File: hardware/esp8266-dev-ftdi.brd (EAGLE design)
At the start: 50 x 50 mm, 58 parts, among them CON1 USBMICRO-NO_CENTER-LONG_PADS

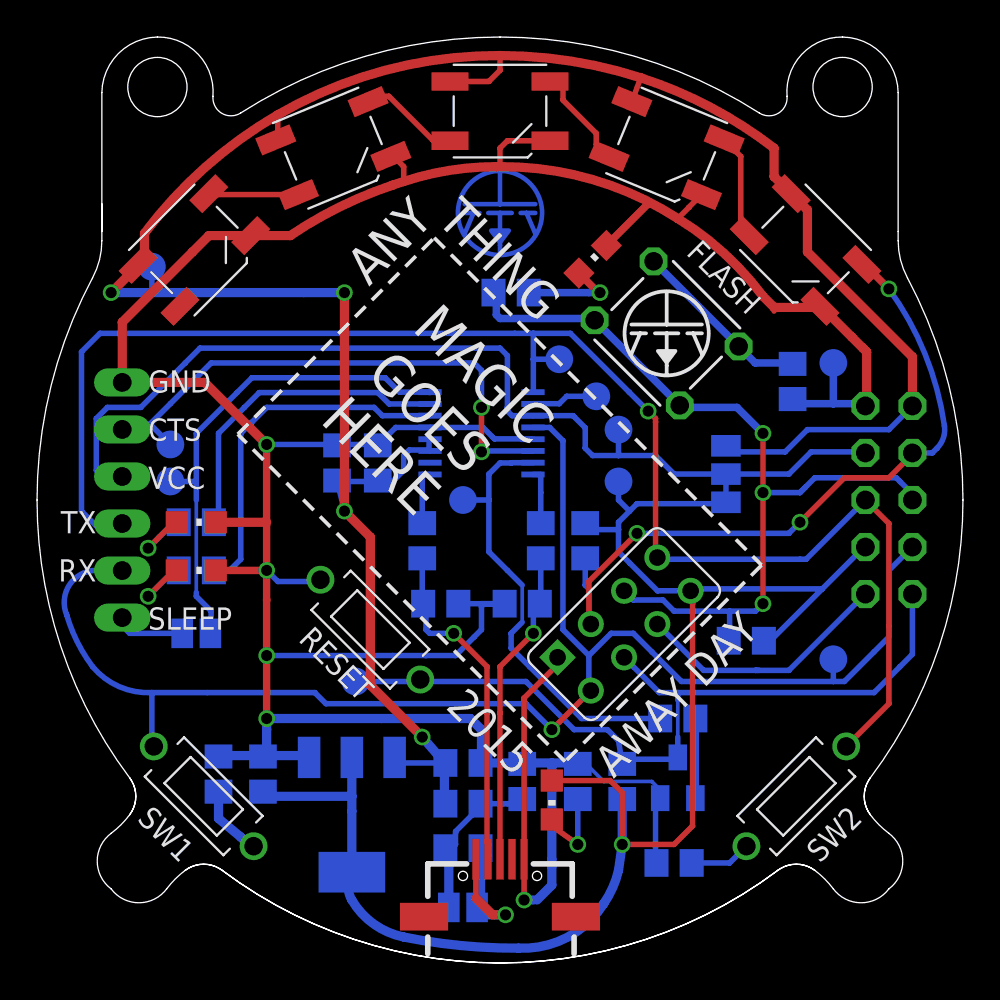
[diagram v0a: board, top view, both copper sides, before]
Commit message: added decoupling caps for leds
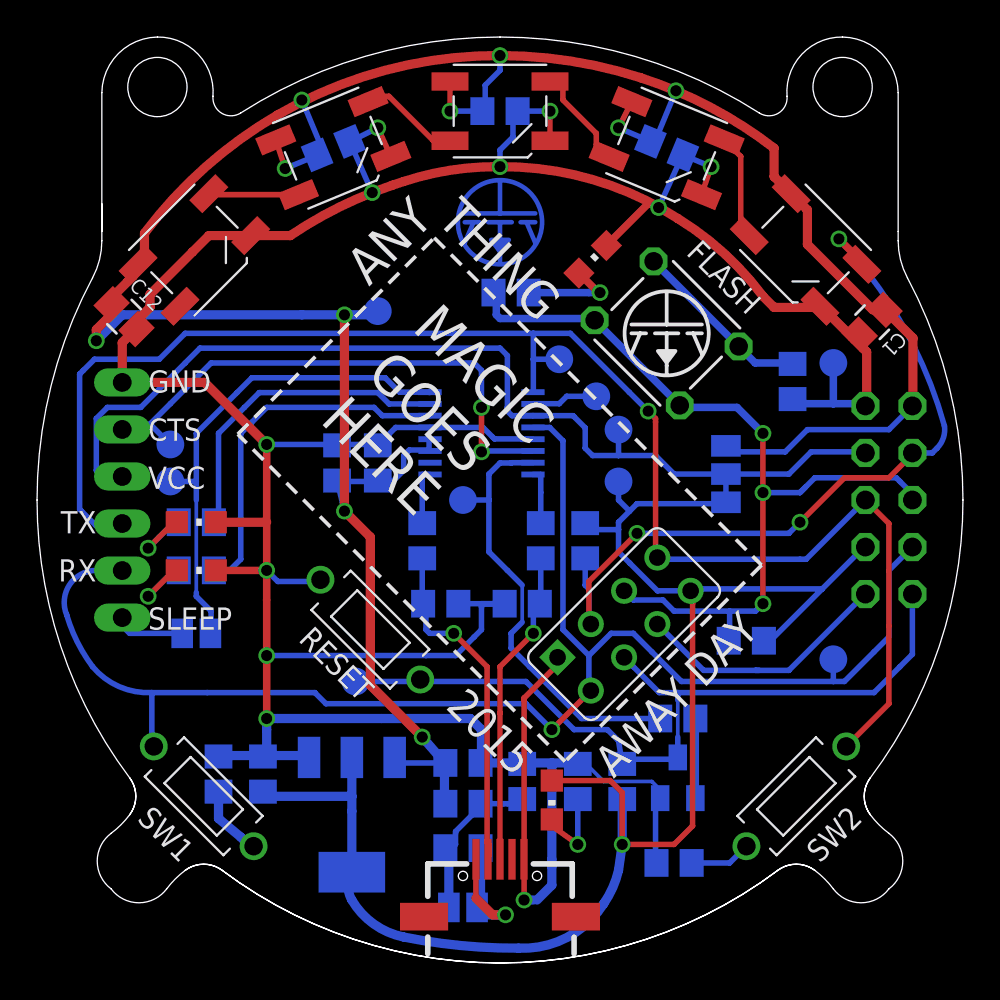
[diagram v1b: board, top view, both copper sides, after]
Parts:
- added C1, C10, C11, C12, C9: 100n, p.peter-rcl:C0805
- moved 5V 12.4 mm to (18.4, 35.2)
- moved U$1 0.50 mm to (25.0, 40.0)
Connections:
- net +5V: now also C1.1, C10.1, C11.1, C12.1, C9.1
- net GND: now also C1.2, C10.2, C11.2, C12.2, C9.2
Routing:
- net +5V: track 134.8 -> 157.2 mm, vias 4 -> 10
- net GND: track 200.6 -> 214.3 mm, vias 5 -> 11
- net IO2: track 39.1 -> 42.8 mm
- net TX: track 84.1 -> 83.5 mm

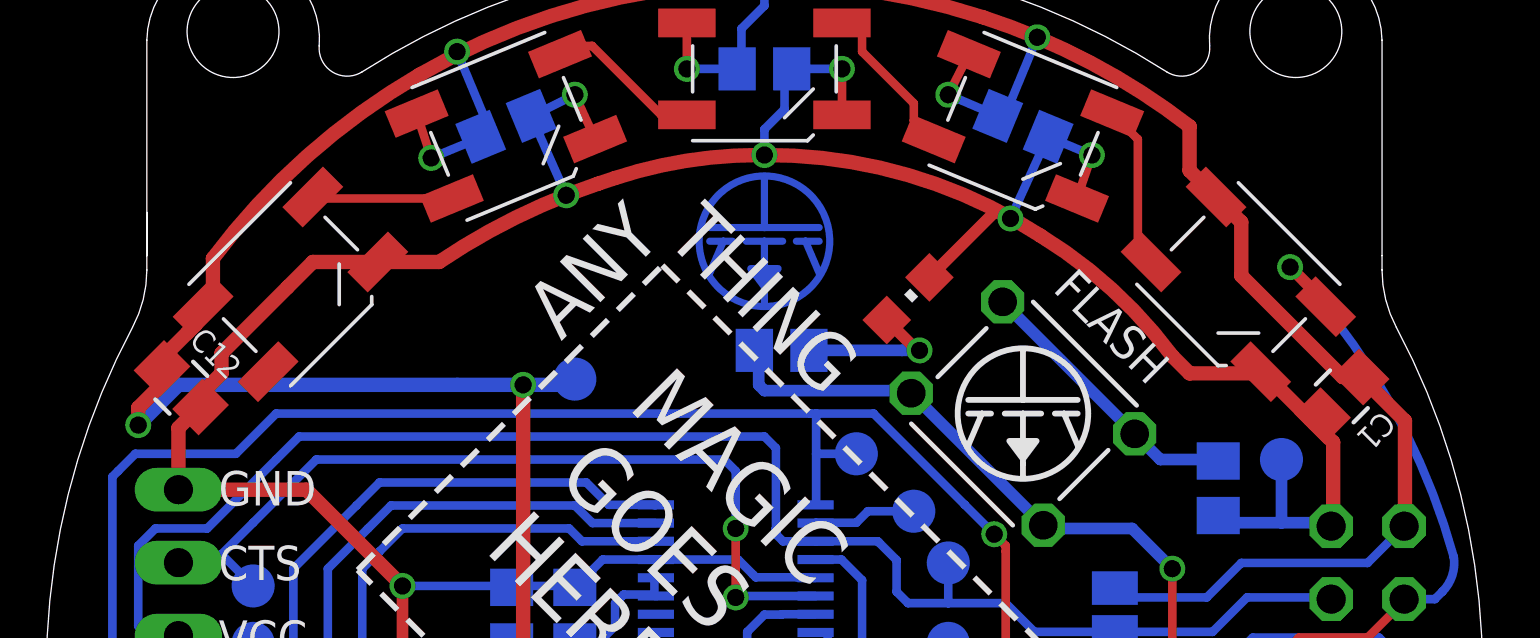
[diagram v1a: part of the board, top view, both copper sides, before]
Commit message: changed bottom values to place layer
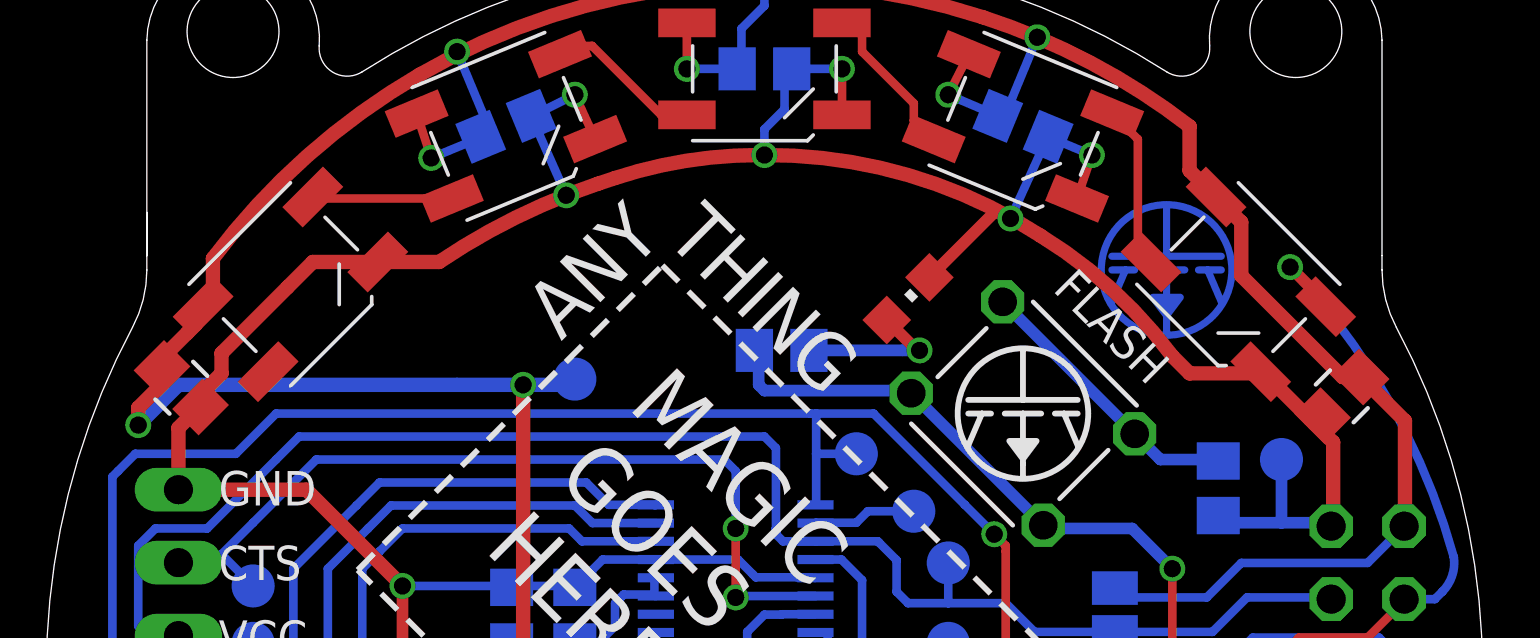
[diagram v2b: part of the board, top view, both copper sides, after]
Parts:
- moved U$1 14.0 mm to (39.0, 39.0)

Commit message: cosmetics
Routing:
- net VCCIO: track 56.8 -> 55.2 mm
- net +3V3: track 89.1 -> 90.3 mm
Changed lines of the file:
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@@
 <setting verticaltext="up"/>
 </settings>
-<grid distance="1" unitdist="mm" unit="mm" style="lines" multiple="1" display="yes" altdistance="0.1" altunitdist="mm" altunit="mm"/>
+<grid distance="0.1" unitdist="mm" unit="mm" style="lines" multiple="1" display="yes" altdistance="0.05" altunitdist="mm" altunit="mm"/>
 <layers>
-<layer number="1" name="Top" color="4" fill="1" visible="no" active="yes"/>
+<layer number="1" name="Top" color="4" fill="1" visible="yes" active="yes"/>
 <layer number="16" name="Bottom" color="1" fill="1" visible="no" active="yes"/>
-<layer number="17" name="Pads" color="2" fill="1" visible="no" active="yes"/>
-<layer number="18" name="Vias" color="2" fill="1" visible="no" active="yes"/>
-<layer number="19" name="Unrouted" color="6" fill="1" visible="no" active="yes"/>
-<layer number="20" name="Dimension" color="15" fill="1" visible="no" active="yes"/>
-<layer number="21" name="tPlace" color="7" fill="1" visible="no" active="yes"/>
+<layer number="17" name="Pads" color="2" fill="1" visible="yes" active="yes"/>
+<layer number="18" name="Vias" color="2" fill="1" visible="yes" active="yes"/>
+<layer number="19" name="Unrouted" color="6" fill="1" visible="yes" active="yes"/>
+<layer number="20" name="Dimension" color="15" fill="1" visible="yes" active="yes"/>
+<layer number="21" name="tPlace" color="7" fill="1" visible="yes" active="yes"/>
 <layer number="22" name="bPlace" color="7" fill="1" visible="no" active="yes"/>
-<layer number="23" name="tOrigins" color="15" fill="1" visible="no" active="yes"/>
+<layer number="23" name="tOrigins" color="15" fill="1" visible="yes" active="yes"/>
 <layer number="24" name="bOrigins" color="15" fill="1" visible="no" active="yes"/>
-<layer number="25" name="tNames" color="7" fill="1" visible="no" active="yes"/>
+<layer number="25" name="tNames" color="7" fill="1" visible="yes" active="yes"/>
 <layer number="26" name="bNames" color="7" fill="1" visible="no" active="yes"/>
 <layer number="27" name="tValues" color="7" fill="1" visible="yes" active="yes"/>
-<layer number="28" name="bValues" color="7" fill="1" visible="yes" active="yes"/>
-<layer number="29" name="tStop" color="7" fill="3" visible="no" active="yes"/>
+<layer number="28" name="bValues" color="7" fill="1" visible="no" active="yes"/>
+<layer number="29" name="tStop" color="7" fill="3" visible="yes" active="yes"/>
 <layer number="30" name="bStop" color="7" fill="6" visible="no" active="yes"/>
 <layer number="31" name="tCream" color="7" fill="4" visible="no" active="yes"/>
@@
 <text x="43.2" y="22" size="1.2" layer="22" font="vector" ratio="15" rot="MR270" align="bottom-center">3V3</text>
 <text x="44.8" y="18.6" size="1.2" layer="22" font="vector" ratio="15" rot="MR270" align="center-left">16</text>
-<text x="48.4" y="27.6" size="1.2" layer="22" font="vector" ratio="15" rot="MR270" align="top-center">2</text>
-<text x="48.4" y="25" size="1.2" layer="22" font="vector" ratio="15" rot="MR270" align="top-center">0</text>
-<text x="48.4" y="22.4" size="1.2" layer="22" font="vector" ratio="15" rot="MR270" align="top-center">RX</text>
+<text x="48.4" y="27.6" size="1" layer="22" font="vector" ratio="15" rot="MR270" align="top-center">2</text>
+<text x="48.4" y="25" size="1" layer="22" font="vector" ratio="15" rot="MR270" align="top-center">0</text>
+<text x="48.4" y="22.7" size="1" layer="22" font="vector" ratio="15" rot="MR270" align="top-center">RX</text>
 <text x="47.2" y="18.8" size="1.2" layer="22" font="vector" ratio="15" rot="MR270" align="center-left">RES</text>
 <text x="17.6" y="36" size="1.7" layer="22" font="vector" ratio="15" rot="MR0">ESP 8266
@@
 </class>
 </classes>
-<designrules name="Elecrow_2-layer_eagle_rule *">
-<description language="de">&lt;b&gt;EAGLE Design Rules&lt;/b&gt;
-&lt;p&gt;
-Die Standard-Design-Rules sind so gewählt, dass sie für
-die meisten Anwendungen passen. Sollte ihre Platine
-besondere Anforderungen haben, treffen Sie die erforderlichen
-Einstellungen hier und speichern die Design Rules unter
-einem neuen Namen ab.</description>
-<description language="en">&lt;b&gt;EAGLE Design Rules&lt;/b&gt;
-&lt;p&gt;
-The default Design Rules have been set to cover
-a wide range of applications. Your particular design
-may have different requirements, so please make the
-necessary adjustments and save your customized
-design rules under a new name.</description>
-<description language="zh">&lt;b&gt;Elecrow EAGLE Design Rules&lt;/b&gt;
-</description>
+<designrules name="dirt_cheap_dirty_boards.v1 *">
+<description language="en">&lt;b&gt;Dirty Cheap Dirty Board Design Rules&lt;/b&gt;
+&lt;br&gt;
+&lt;br&gt;Min width/Spacing: 5/5mil
+&lt;br&gt;Min diameter of finished hole 12mil</description>
 <param name="layerSetup" value="(1*16)"/>
-<param name="mtCopper" value="0.035mm 0.035mm 0.035mm 0.035mm 0.035mm 0.035mm 0.035mm 0.035mm 0.035mm 0.035mm 0.035mm 0.035mm 0.035mm 0.035mm 0.035mm 0.035mm"/>
-<param name="mtIsolate" value="1.5mm 0.15mm 0.2mm 0.15mm 0.2mm 0.15mm 0.2mm 0.15mm 0.2mm 0.15mm 0.2mm 0.15mm 0.2mm 0.15mm 0.2mm"/>
-<param name="mdWireWire" value="6mil"/>
-<param name="mdWirePad" value="6mil"/>
-<param name="mdWireVia" value="6mil"/>
-<param name="mdPadPad" value="6mil"/>
-<param name="mdPadVia" value="6mil"/>
-<param name="mdViaVia" value="6mil"/>
+<param name="mtCopper" value="0.035mm 0.0175mm 0.035mm 0.035mm 0.035mm 0.035mm 0.035mm 0.035mm 0.035mm 0.035mm 0.035mm 0.035mm 0.035mm 0.035mm 0.0175mm 0.035mm"/>
+<param name="mtIsolate" value="1.5mm 1.1mm 0.2mm 0.15mm 0.2mm 0.15mm 0.2mm 0.15mm 0.2mm 0.15mm 0.2mm 0.15mm 0.2mm 0.15mm 0.2mm"/>
+<param name="mdWireWire" value="5mil"/>
+<param name="mdWirePad" value="5mil"/>
+<param name="mdWireVia" value="5mil"/>
+<param name="mdPadPad" value="5mil"/>
+<param name="mdPadVia" value="5mil"/>
+<param name="mdViaVia" value="5mil"/>
 <param name="mdSmdPad" value="0mil"/>
 <param name="mdSmdVia" value="0mil"/>
@@
 <param name="mdDrill" value="10mil"/>
 <param name="mdSmdStop" value="0mil"/>
-<param name="msWidth" value="6mil"/>
+<param name="msWidth" value="5mil"/>
 <param name="msDrill" value="12mil"/>
 <param name="msMicroVia" value="12mil"/>
 <param name="msBlindViaRatio" value="0.5"/>
-<param name="rvPadTop" value="0.25"/>
-<param name="rvPadInner" value="0.25"/>
-<param name="rvPadBottom" value="0.25"/>
+<param name="rvPadTop" value="0.3"/>
+<param name="rvPadInner" value="0.3"/>
+<param name="rvPadBottom" value="0.3"/>
 <param name="rvViaOuter" value="0.25"/>
 <param name="rvViaInner" value="0.25"/>
@@
 <param name="rvMicroViaInner" value="0.25"/>
 <param name="rlMinPadTop" value="10mil"/>
-<param name="rlMaxPadTop" value="20mil"/>
+<param name="rlMaxPadTop" value="30mil"/>
 <param name="rlMinPadInner" value="10mil"/>
-<param name="rlMaxPadInner" value="20mil"/>
+<param name="rlMaxPadInner" value="30mil"/>
 <param name="rlMinPadBottom" value="10mil"/>
-<param name="rlMaxPadBottom" value="20mil"/>
+<param name="rlMaxPadBottom" value="30mil"/>
 <param name="rlMinViaOuter" value="6mil"/>
 <param name="rlMaxViaOuter" value="20mil"/>
@@
 <param name="mlMinCreamFrame" value="0mil"/>
 <param name="mlMaxCreamFrame" value="0mil"/>
-<param name="mlViaStopLimit" value="100mil"/>
+<param name="mlViaStopLimit" value="25mil"/>
 <param name="srRoundness" value="0"/>
 <param name="srMinRoundness" value="0mil"/>
@@
 <wire x1="32" y1="21.6" x2="31.4" y2="22.2" width="0.3" layer="16"/>
 <wire x1="29.55" y1="23.4" x2="29.6" y2="23.75" width="0.3" layer="16"/>
-<wire x1="37.124" y1="24.8" x2="37.2" y2="24.876" width="0.3" layer="16"/>
 <wire x1="42.4" y1="20.2" x2="35.39605" y2="20.2" width="0.3" layer="16"/>
 <wire x1="35.39605" y1="20.2" x2="35.2921" y2="20.09605" width="0.3" layer="16"/>
@@
 <wire x1="42.4" y1="20.2" x2="39.6" y2="17.4" width="0.3" layer="16"/>
 <wire x1="39.6" y1="17.4" x2="39.25" y2="17.4" width="0.3" layer="16"/>
+<wire x1="37.124" y1="24.8" x2="37.2" y2="24.9" width="0.3" layer="16"/>
+<wire x1="37.2" y1="24.9" x2="37.2" y2="26.1" width="0.3" layer="16"/>
 </signal>
 <signal name="N$9">
@@
 <wire x1="29" y1="29.5" x2="28.947" y2="29.553" width="0.3" layer="16"/>
 <wire x1="28.947" y1="29.553" x2="26.779" y2="29.553" width="0.3" layer="16"/>
-<wire x1="37.2" y1="24.8" x2="37.2" y2="26.4" width="0.3" layer="16"/>
 <contactref element="VCC" pad="TP"/>
 <wire x1="31.4" y1="28.8" x2="31.4" y2="27.4" width="0.3" layer="16"/>

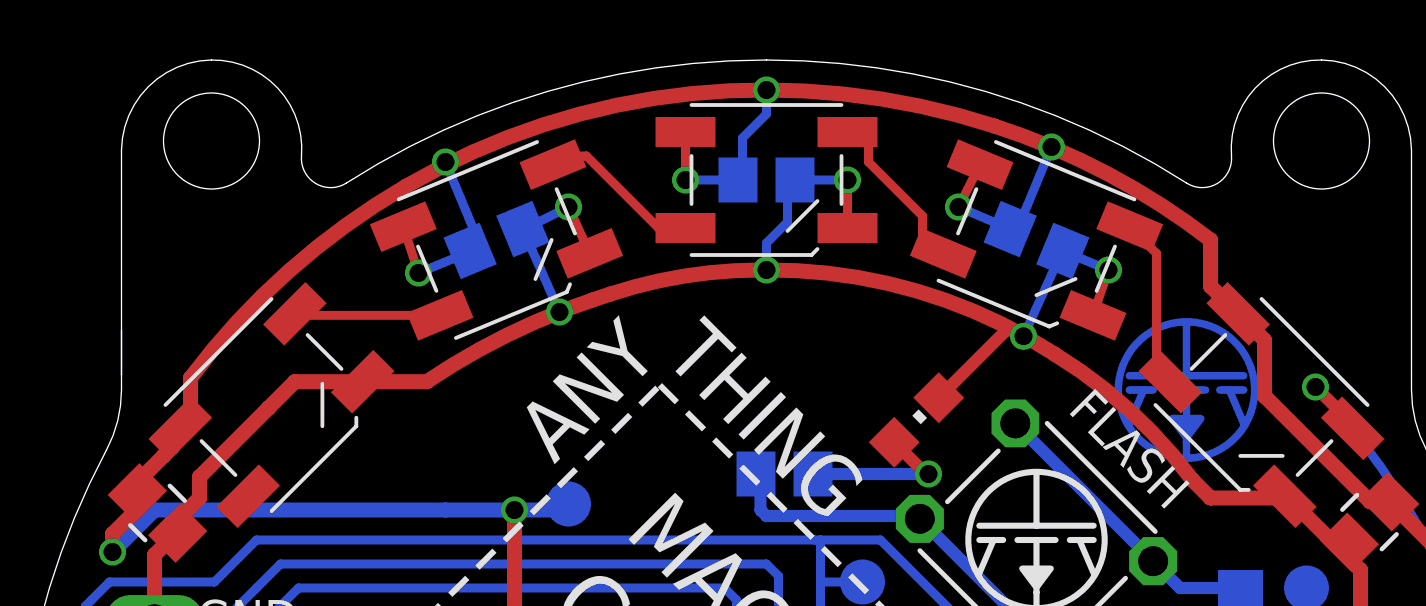
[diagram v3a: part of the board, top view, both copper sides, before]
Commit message: Increasing distance between pads and signals
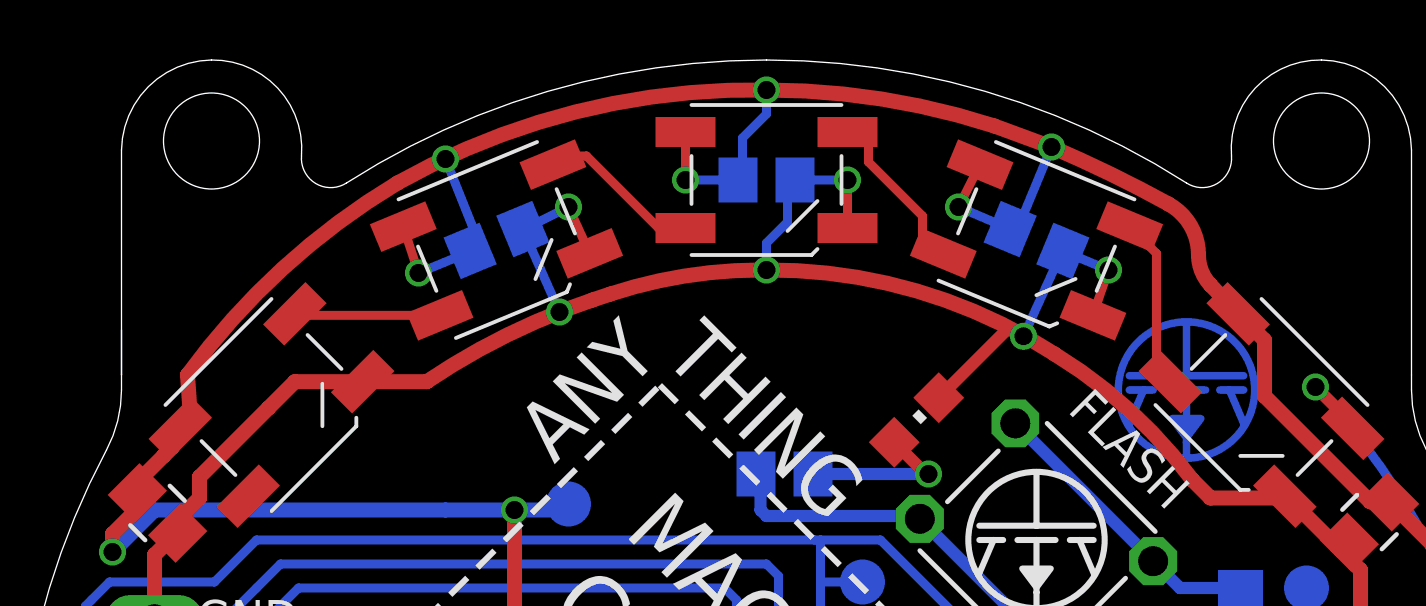
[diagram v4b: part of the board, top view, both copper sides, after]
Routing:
- net +5V: track 157.2 -> 155.5 mm
